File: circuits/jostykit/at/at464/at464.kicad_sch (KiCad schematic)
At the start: 3 parts, among them U1 TL084, U2 TL084, U3 CA3140

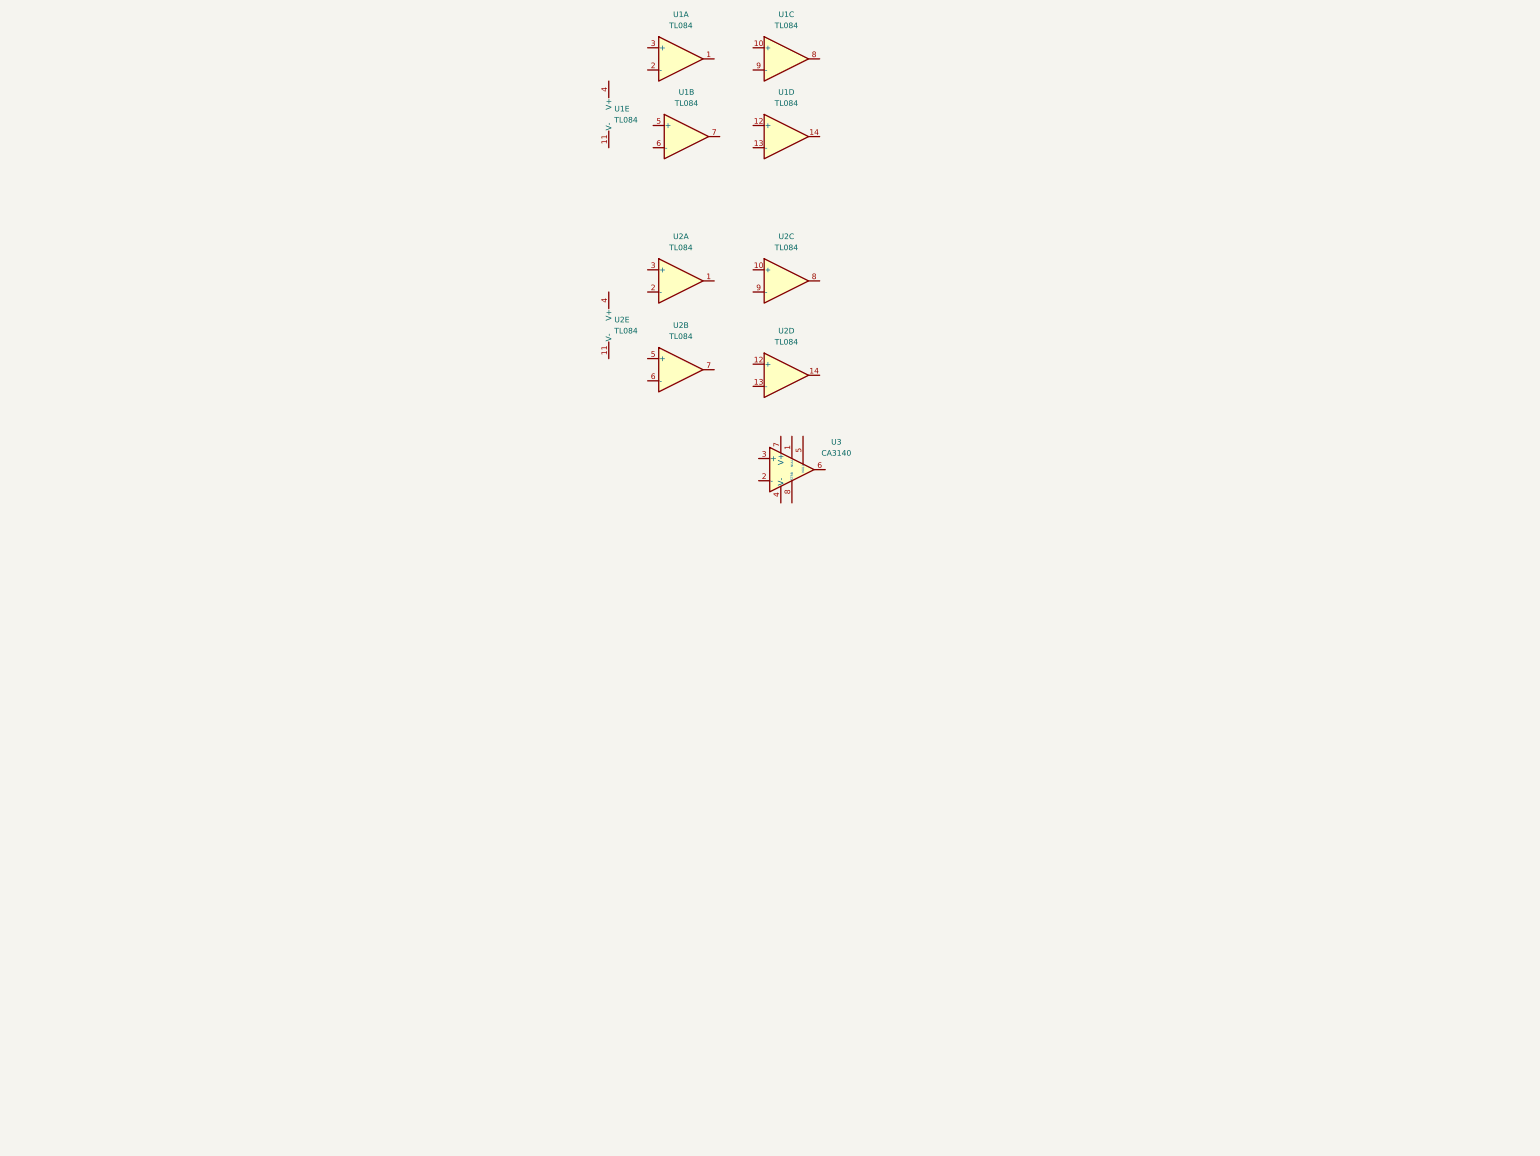
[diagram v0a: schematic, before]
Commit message: Updating the AT464 JostyKit circuit with some new custom symbols
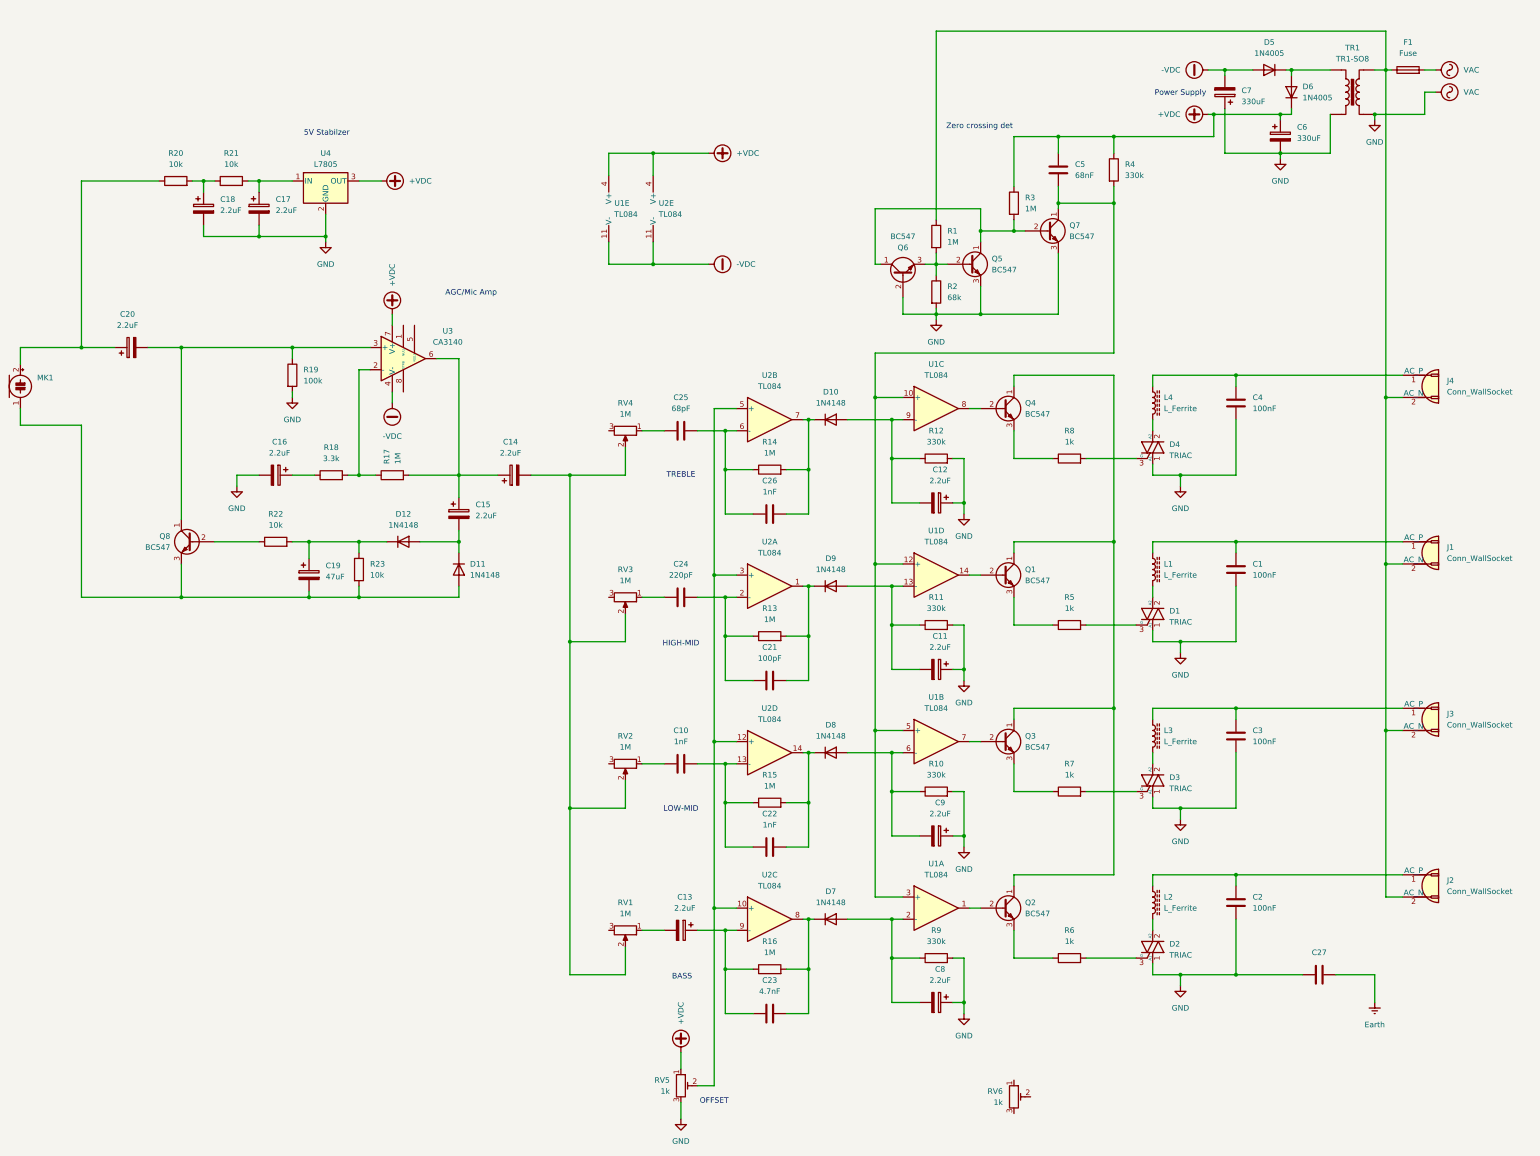
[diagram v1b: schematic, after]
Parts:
- added C1, C2, C3, C4: 100nF, symbol Device:C
- added C10, C22, C26: 1nF, symbol Device:C
- added C11, C12, C13, C14, C15, C16, C17, C18, C20, C8, C9: 2.2uF, symbol Device:C_Polarized
- added C19: 47uF, symbol Device:C_Polarized
- added C21: 100pF, symbol Device:C
- added C23: 4.7nF, symbol Device:C
- added C24: 220pF, symbol Device:C
- added C25: 68pF, symbol Device:C
- added C27: (no value), symbol Device:C
- added C5: 68nF, symbol Device:C
- added C6, C7: 330uF, symbol Device:C_Polarized
- added D1, D2, D3, D4: TRIAC, symbol Device:Q_TRIAC_A1A2G
- added D10, D11, D12, D7, D8, D9: 1N4148, symbol Device:D
- added D5, D6: 1N4005, symbol Device:D
- added F1: Fuse, symbol Device:Fuse
- added J1, J2, J3, J4: Conn_WallSocket, symbol Connector:Conn_WallSocket
- added L1, L2, L3, L4: L_Ferrite, symbol Device:L_Ferrite
- added MK1: ~, symbol Device:Microphone_Condenser
- added Q1, Q2, Q3, Q4, Q5, Q6, Q7, Q8: BC547, Package_TO_SOT_THT:TO-92_Inline, symbol Transistor_BJT:BC547
- added R1, R13, R14, R15, R16, R17, R3: 1M, symbol Device:R
- added R10, R11, R12, R4, R9: 330k, symbol Device:R
- added R18: 3.3k, symbol Device:R
- added R19: 100k, symbol Device:R
- added R2: 68k, symbol Device:R
- added R20, R21, R22, R23: 10k, symbol Device:R
- added R5, R6, R7, R8: 1k, symbol Device:R
- added RV1, RV2, RV3, RV4: 1M, symbol Device:R_Potentiometer
- added RV5, RV6: 1k, symbol Device:R_Potentiometer_Trim
- added TR1: TR1-SO8, symbol Transformer:TR1-SO8
- added U4: L7805, symbol Regulator_Linear:L7805
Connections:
- net at U2.1: now also C21.2, D9.1 (K), R13.2
- net at U2.2 (-): now also C21.1, C24.2, R13.1
- net at U2.3 (+): now also U2.10 (+), U2.12 (+), U2.5 (+), RV5.2
- net at U1.10 (+): now also U1.12 (+), U1.3 (+), U1.5 (+), C5.2, Q7.1 (C), R4.2
- net at U1.8: now also Q4.2 (B)
- net at U1.9 (-): now also C12.2, D10.2 (A), R12.1
- net at U1.1: now also Q2.2 (B)
- net at U1.2 (-): now also C8.2, D7.2 (A), R9.1
- net -VDC: now reaches U2.11 (V-)
- net -VDC: now also U1.11 (V-), U3.4 (V-), C7.2, D5.2 (A)
- net +VDC: now reaches U2.4 (V+)
- net +VDC: now also U1.4 (V+), U3.7 (V+), C5.1, C6.1, D6.1 (K), R3.1, R4.1, RV5.1, U4.3 (OUT)
- net at U1.13 (-): now also C11.2, D9.2 (A), R11.1
- net at U1.14: now also Q1.2 (B)
- net at U1.6 (-): now also C9.2, D8.2 (A), R10.1
- net at U1.7: now also Q3.2 (B)
- net at U3.2 (-): now also R17.1, R18.2
- net at U3.3 (+): now also C20.2, Q8.1 (C), R19.1
- net at U3.6: now also C14.1, C15.1, R17.2
- net at U2.6 (-): now also C25.2, C26.1, R14.1
- net at U2.7: now also C26.2, D10.1 (K), R14.2
- net at U2.13 (-): now also C10.2, C22.1, R15.1
- net at U2.14: now also C22.2, D8.1 (K), R15.2
- net at U2.8: now also C23.2, D7.1 (K), R16.2
- net at U2.9 (-): now also C13.1, C23.1, R16.1
- new net: C19.2, D11.2 (A), MK1.1 (-), Q8.3 (E), R23.2
- new net: C20.1, MK1.2 (+), R20.1
- new net: C10.1, RV2.1
- new net: Q3.3 (E), R7.1
- new net: D3.3 (G), R7.2
- new net: C4.1, J4.1 (AC_P), L4.1
- new net: F1.1, J1.2 (AC_N), J2.2 (AC_N), J3.2 (AC_N), J4.2 (AC_N), R1.1, TR1.8
- new net: Q5.2 (B), Q6.3 (E), R1.2, R2.1
- new net: C24.1, RV3.1
- new net: C14.2, RV1.2, RV2.2, RV3.2, RV4.2
- new net: C18.1, R20.2, R21.1
- new net: C17.1, R21.2, U4.1 (IN)
- new net: C16.1, R18.1
- new net: C2.1, J2.1 (AC_P), L2.1
- new net: C15.2, D11.1 (K), D12.2 (A)
- new net: D5.1 (K), D6.2 (A), TR1.1
- new net: C13.2, RV1.1
- new net: C3.1, J3.1 (AC_P), L3.1
- new net: Q5.1 (C), Q6.1 (C), Q7.2 (B), R3.2
- new net: C25.1, RV4.1
- new net: C19.1, D12.1 (K), R22.2, R23.1
- new net: D3.2 (A2), L3.2
- new net: Q2.3 (E), R6.1
- new net: D2.3 (G), R6.2
- new net: D4.2 (A2), L4.2
- new net: Q1.3 (E), R5.1
- new net: D1.3 (G), R5.2
- new net: Q4.3 (E), R8.1
- new net: D4.3 (G), R8.2
- new net: Q1.1 (C), Q2.1 (C), Q3.1 (C), Q4.1 (C)
- new net: Q8.2 (B), R22.1
- new net: D2.2 (A2), L2.2
- new net: C1.1, J1.1 (AC_P), L1.1
- new net: D1.2 (A2), L1.2
- new net Earth: C27.2
- new net GND: C1.2, C11.1, C12.1, C16.2, C17.2, C18.2, C2.2, C27.1, C3.2, C4.2, C6.2, C7.1, C8.1, C9.1, D1.1 (A1), D2.1 (A1), D3.1 (A1), D4.1 (A1), F1.2, Q5.3 (E), Q6.2 (B), Q7.3 (E), R10.2, R11.2, R12.2, R19.2, R2.2, R9.2, RV5.3, TR1.4, TR1.5, U4.2 (GND)
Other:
- note added: "5V Stabilzer"
- note added: "AGC/Mic Amp"
- note added: "BASS"
- note added: "HIGH-MID"
- note added: "LOW-MID"
- note added: "OFFSET"
- note added: "Power Supply"
- note added: "TREBLE"
- note added: "Zero crossing det"
- title: (none) -> AT464 by Jan Soelberg

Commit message: Splitting AT464 into concept circuits for verification
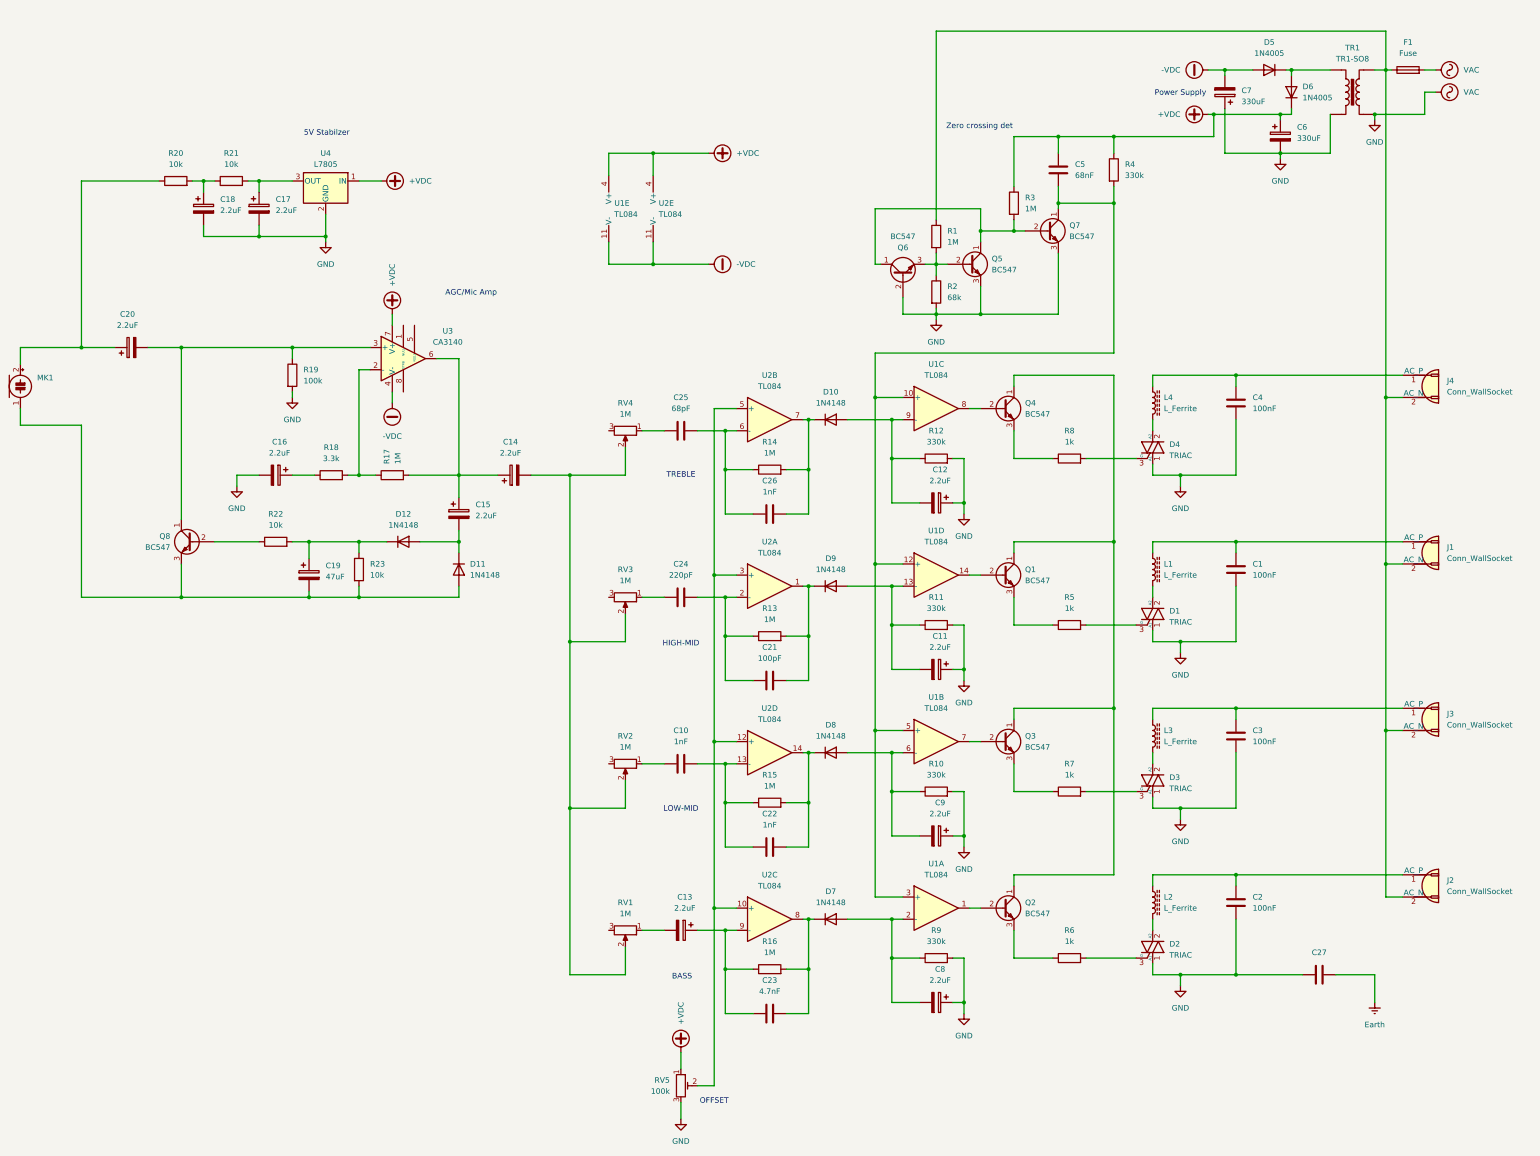
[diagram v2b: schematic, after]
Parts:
- removed RV6: 1k, symbol Device:R_Potentiometer_Trim
- RV5: value 1k -> 100k
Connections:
- net +VDC: now also U4.1 (IN); no longer U4.3 (OUT)
- net at C17.1, R21.2: now also U4.3 (OUT); no longer U4.1 (IN)
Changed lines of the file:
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@@
 	)
 	(junction
-		(at 340.36 50.8)
+		(at 106.68 57.15)
 		(diameter 0)
 		(color 0 0 0 0)
 	)
 	(junction
-		(at 106.68 57.15)
+		(at 340.36 50.8)
 		(diameter 0)
 		(color 0 0 0 0)
@@
 	(wire
 		(pts
-			(xy 106.68 57.15) (xy 114.3 57.15)
-		)
-		(stroke
-			(width 0)
-			(type default)
-		)
-	)
-	(wire
-		(pts
 			(xy 311.15 200.66) (xy 311.15 198.12)
 		)
@@
 	(wire
 		(pts
+			(xy 129.54 57.15) (xy 134.62 57.15)
+		)
+		(stroke
+			(width 0)
+			(type default)
+		)
+	)
+	(wire
+		(pts
 			(xy 330.2 111.76) (xy 330.2 124.46)
 		)
@@
 	(wire
 		(pts
+			(xy 106.68 57.15) (xy 114.3 57.15)
+		)
+		(stroke
+			(width 0)
+			(type default)
+		)
+	)
+	(wire
+		(pts
 			(xy 118.11 152.4) (xy 118.11 151.13)
 		)
@@
 	(wire
 		(pts
-			(xy 129.54 57.15) (xy 134.62 57.15)
-		)
-		(stroke
-			(width 0)
-			(type default)
-		)
-	)
-	(wire
-		(pts
 			(xy 215.9 185.42) (xy 210.82 185.42)
 		)
@@
 			)
 		)
-		(property "Value" "1k"
+		(property "Value" "100k"
 			(at 200.66 265.4299 0)
 			(effects
@@
 	)
 	(symbol
-		(lib_id "Device:R_Potentiometer_Trim")
-		(at 279.4 266.7 0)
-		(unit 1)
-		(exclude_from_sim no)
-		(in_bom yes)
-		(on_board yes)
-		(dnp no)
-		(fields_autoplaced yes)
-		(property "Reference" "RV6"
-			(at 276.86 265.4299 0)
-			(effects
-				(font
-					(size 1.27 1.27)
-				)
-				(justify right)
-			)
-		)
-		(property "Value" "1k"
-			(at 276.86 267.9699 0)
-			(effects
-				(font
-					(size 1.27 1.27)
-				)
-				(justify right)
-			)
-		)
-		(property "Footprint" ""
-			(at 279.4 266.7 0)
-			(effects
-				(font
-					(size 1.27 1.27)
-				)
-				(hide yes)
-			)
-		)
-		(property "Datasheet" "~"
-			(at 279.4 266.7 0)
-			(effects
-				(font
-					(size 1.27 1.27)
-				)
-				(hide yes)
-			)
-		)
-		(property "Description" "Trim-potentiometer"
-			(at 279.4 266.7 0)
-			(effects
-				(font
-					(size 1.27 1.27)
-				)
-				(hide yes)
-			)
-		)
-		(pin "2"
-		)
-		(pin "3"
-		)
-		(pin "1"
-		)
-		(instances
-			(project "at464"
-				(path "/9ec3024c-09fb-4447-8387-a93390aba070"
-					(reference "RV6")
-					(unit 1)
-				)
-			)
-		)
-	)
-	(symbol
 		(lib_id "power:GND")
 		(at 267.97 133.35 0)
@@
 		(lib_id "Regulator_Linear:L7805")
 		(at 121.92 57.15 0)
+		(mirror y)
 		(unit 1)
 		(exclude_from_sim no)
@@
 		(on_board yes)
 		(dnp no)
-		(fields_autoplaced yes)
 		(property "Reference" "U4"
 			(at 121.92 50.8 0)
@@
 		)
 		(property "Footprint" ""
-			(at 122.555 60.96 0)
+			(at 121.285 60.96 0)
 			(effects
 				(font
